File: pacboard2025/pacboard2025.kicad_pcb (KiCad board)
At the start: 4 copper layers, 80 x 85 mm, 28 parts, among them J1 XT30 Male Connector, U2 D24V50F5, U3 ProS3

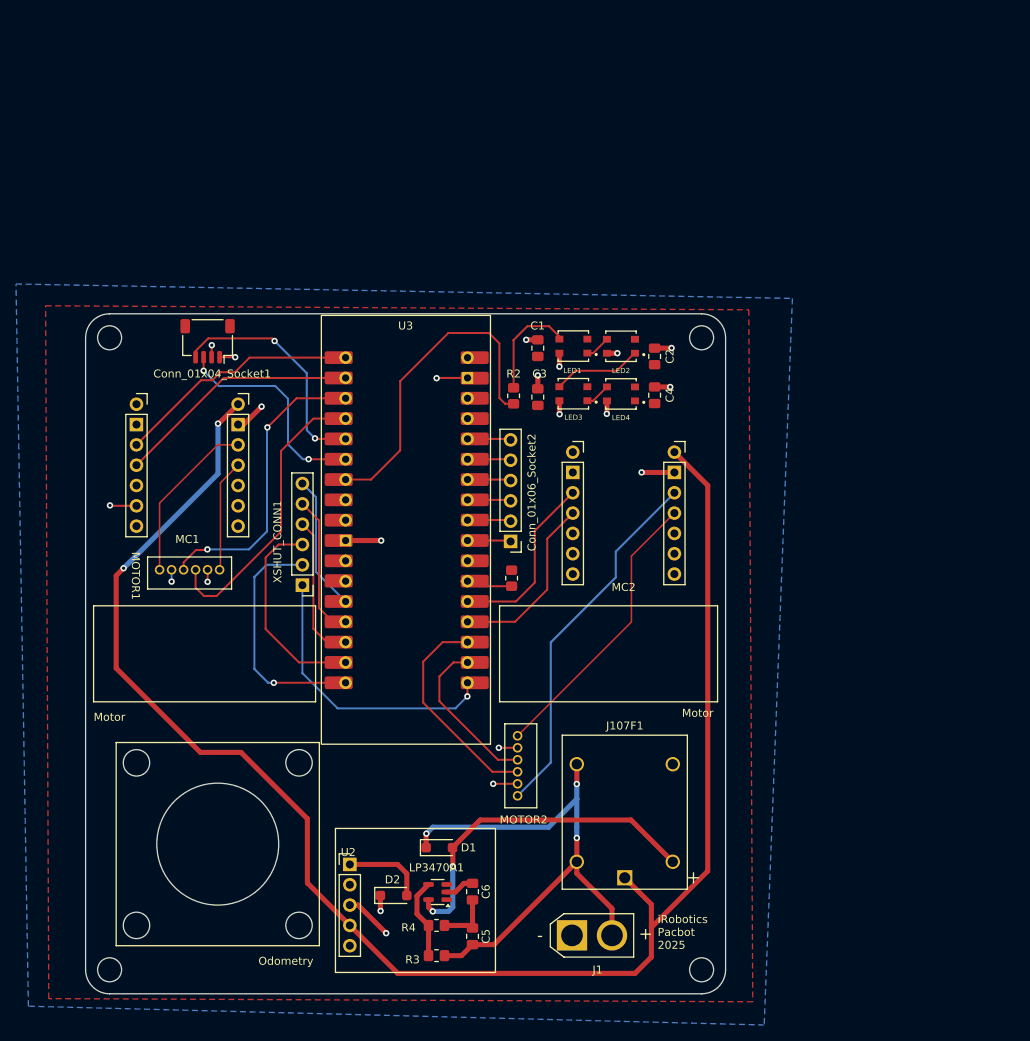
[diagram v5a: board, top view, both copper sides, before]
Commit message: added testpoints
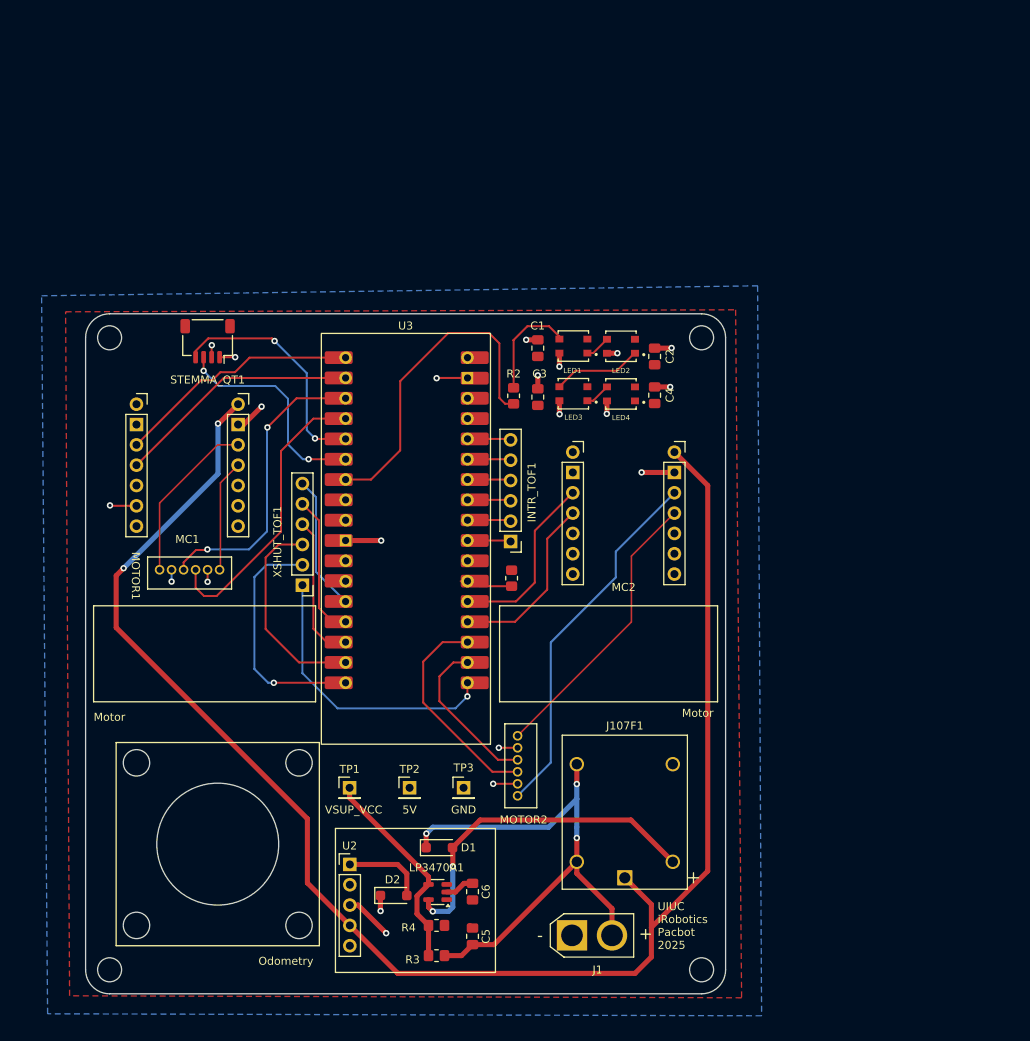
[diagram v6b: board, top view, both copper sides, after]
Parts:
- added TP1: VSUP_VCC, Connector_PinHeader_2.54mm:PinHeader_1x01_P2.54mm_Vertical, F.Cu at (113.0, 154.2)
- added TP2: 5V, Connector_PinHeader_2.54mm:PinHeader_1x01_P2.54mm_Vertical, F.Cu at (120.5, 154.2)
- added TP3: GND, Connector_PinHeader_2.54mm:PinHeader_1x01_P2.54mm_Vertical, F.Cu at (127.2, 154.2)
- INTR_TOF1: renamed from Conn_01x06_Socket2; value TOF_INTR_CONN -> Conn_01x06_Socket2
- renumbered Conn_01x04_Socket1 to STEMMA_QT1, XSHUT_CONN1 to XSHUT_TOF1
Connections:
- C5 pad 1: GNDREF -> /GND
- C6 pad 2: GNDREF -> /GND
- R4 pad 2: GNDREF -> /GND
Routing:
- net Net-(LP3470A1-VCC): track 10.1 -> 26.3 mm
- net GNDREF: track 7.15 -> 0.00 mm
- net /12V: track 202.9 -> 200.0 mm
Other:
- board text added: "5V"
- board text added: "GND"
- board text added: "UIUC iRobotics Pacbot 2025"
- board text added: "VSUP_VCC"
- board text removed: "iRobotics Pacbot 2025"

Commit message: some more changes
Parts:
- moved U2 46.2 mm to (144.6, 130.1)
- moved D1 46.2 mm to (156.0, 122.9)
- moved LED2 46.2 mm to (178.5, 65.3)
- moved MC2 46.2 mm to (178.8, 72.7)
- moved R1 46.2 mm to (164.8, 94.3)
- moved R4 46.2 mm to (155.4, 137.7)
- moved C2 46.2 mm to (182.7, 66.6)
- moved C4 46.2 mm to (182.7, 71.5)
- moved D2 46.2 mm to (150.2, 128.9)
- moved INTR_TOF1 46.2 mm to (164.7, 89.7)
- moved J107F1 46.2 mm to (178.9, 131.8)
- moved LED1 46.2 mm to (172.5, 65.3)
- moved LED3 46.2 mm to (172.5, 71.3)
- moved LED4 46.2 mm to (178.5, 71.3)
- moved LP3470A1 46.2 mm to (155.6, 133.6)
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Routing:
- net /LED_DATA: track 41.3 -> 37.8 mm
- net /1_PWM1: track 29.8 -> 30.7 mm
- net /XSHUT_TOF5: track 29.4 -> 28.6 mm
- net /XSHUT_TOF4: track 25.1 -> 24.3 mm
- net /GND: track 30.2 -> 30.8 mm, vias 8 -> 71
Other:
- board text added: "uh oh..."

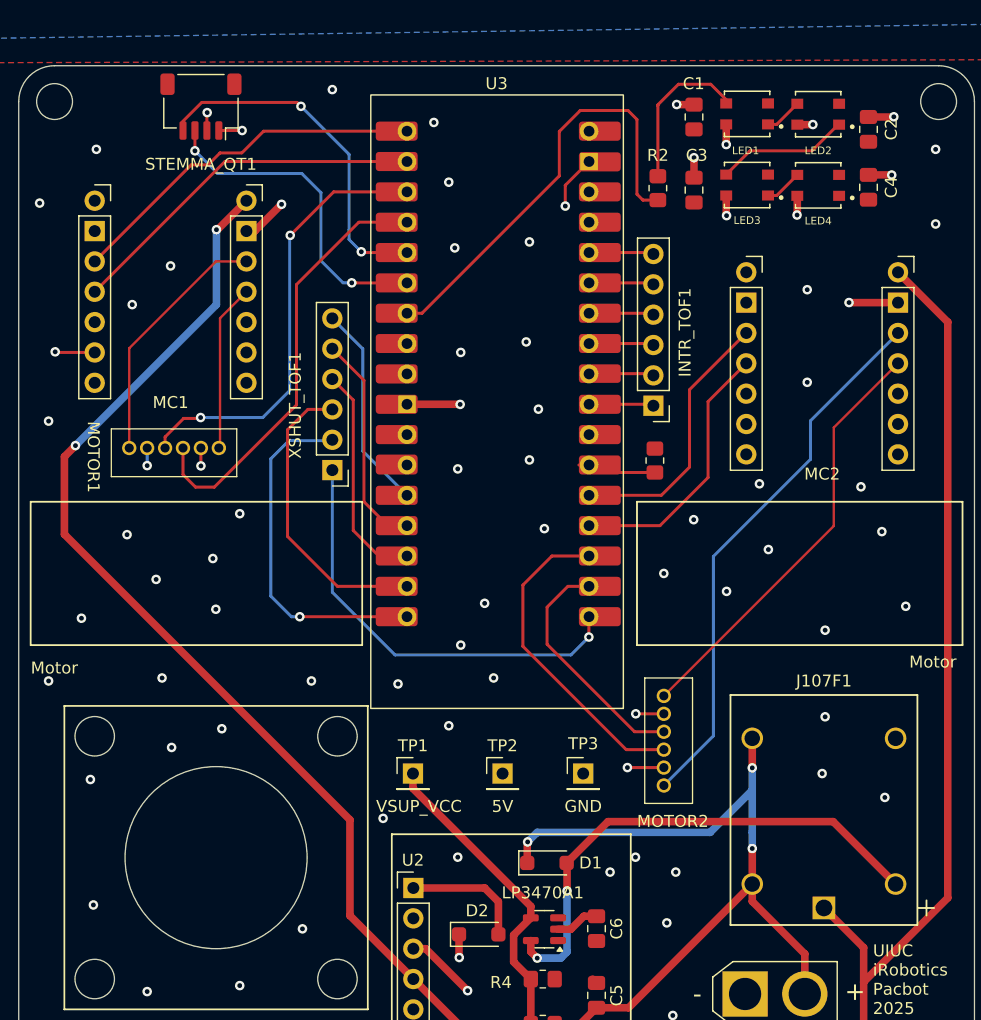
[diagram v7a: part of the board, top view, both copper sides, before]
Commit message: fixed neopixels, all ready to go?
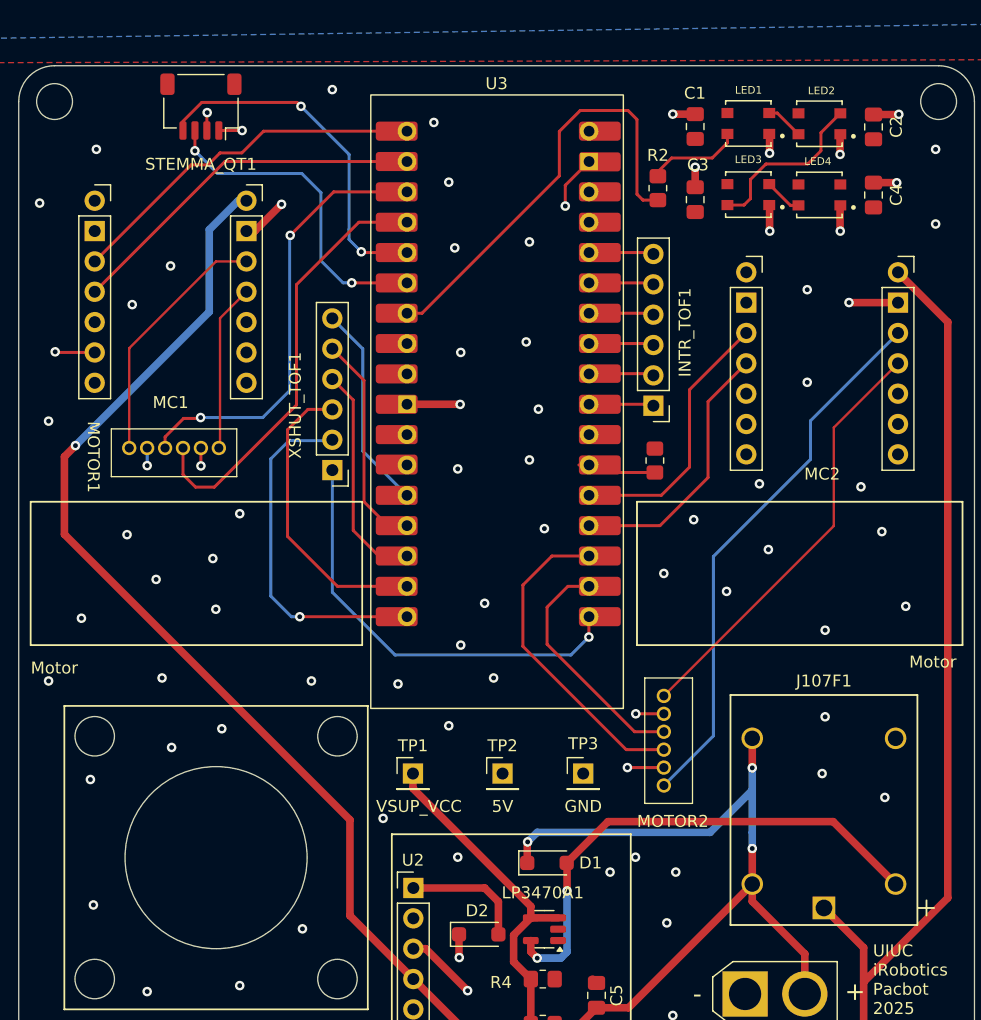
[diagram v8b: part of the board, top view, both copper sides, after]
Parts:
- removed C6: 0.1uF, Capacitor_SMD:C_0805_2012Metric_Pad1.18x1.45mm_HandSolder
- moved C1 0.81 mm to (168.2, 66.4)
- moved LED2 0.81 mm to (178.6, 66.1)
- moved C3 0.81 mm to (168.2, 72.5)
- moved LED1 0.81 mm to (172.6, 66.1)
- moved LED3 0.81 mm to (172.6, 72.1)
- moved LED4 0.81 mm to (178.6, 72.1)
- moved C4 0.77 mm to (183.1, 72.1)
- moved C2 0.47 mm to (183.1, 66.4)
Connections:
- LED1 pad 1: Net-(LED1-DOUT) -> /GND
- LED1 pad 2: /GND -> Net-(LED1-DIN)
- LED1 pad 3: Net-(LED1-DIN) -> /5V
- LED1 pad 4: /5V -> Net-(LED1-DOUT)
- LED2 pad 1: Net-(LED2-DOUT) -> /GND
- LED2 pad 2: /GND -> Net-(LED1-DOUT)
- LED2 pad 3: Net-(LED1-DOUT) -> /5V
- LED2 pad 4: /5V -> Net-(LED2-DOUT)
- LED3 pad 1: Net-(LED3-DOUT) -> /GND
- LED3 pad 2: /GND -> Net-(LED2-DOUT)
- LED3 pad 3: Net-(LED2-DOUT) -> /5V
- LED3 pad 4: /5V -> Net-(LED3-DOUT)
- LED4 pad 1: unconnected-(LED4-DOUT-Pad1) -> /GND
- LED4 pad 2: /GND -> Net-(LED3-DOUT)
- LED4 pad 3: Net-(LED3-DOUT) -> /5V
- LED4 pad 4: /5V -> unconnected-(LED4-DOUT-Pad4)
- LP3470A1 pad 2: Net-(LP3470A1-GND) -> /GND
- LP3470A1 pad 3: unconnected-(LP3470A1-VCC1-Pad3) -> Net-(LP3470A1-VCC)
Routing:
- net Net-(LED1-DIN): track 13.3 -> 7.94 mm
- net Net-(LP3470A1-GND): track 3.68 -> 0.00 mm
- net Net-(LED2-DOUT): track 11.2 -> 14.5 mm
- net Net-(LP3470A1-VCC): track 26.3 -> 28.5 mm
- net /5V: track 15.5 -> 17.1 mm
- net /12V: track 200.0 -> 200.3 mm, vias 2 -> 1
